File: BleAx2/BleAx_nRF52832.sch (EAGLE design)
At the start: 42 parts, among them CN1 6p-2.54, J1 2.0MM-90D, U1 NRF52832, U2 MCP73832T-2ACI/OT-SOT23-5, U4 MIC5225-3.3, X1 FA-128, X2 32.768kHz

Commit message: halfway?
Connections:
- net BTTN_01: now also U1.P0.10/NFC2@12; no longer U1.P0.31@43
- net LIS_CS: now also U1.P0.06@08; no longer U1.P0.07@09
- net LIS_INT1: now also U1.P0.05/AIN3@07; no longer U1.P0.06@08
- net MISO_01: now also U1.P0.07@09; no longer U1.P0.08@10
- net MOSI_01: now also U1.P0.08@10; no longer U1.P0.09/NFC1@11
- net SCK_01: now also U1.P0.09/NFC1@11; no longer U1.P0.10/NFC2@12
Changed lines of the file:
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@@
 </segment>
 <segment>
-<wire x1="88.9" y1="78.74" x2="66.04" y2="78.74" width="0.1524" layer="91"/>
-<pinref part="U1" gate="U$1" pin="P0.08@10"/>
-<label x="66.04" y="78.74" size="1.27" layer="95" rot="R180" xref="yes"/>
+<wire x1="88.9" y1="81.28" x2="63.5" y2="81.28" width="0.1524" layer="91"/>
+<pinref part="U1" gate="U$1" pin="P0.07@09"/>
+<label x="63.5" y="81.28" size="1.27" layer="95" rot="R180" xref="yes"/>
 </segment>
 </net>
@@
 </segment>
 <segment>
-<wire x1="66.04" y1="73.66" x2="88.9" y2="73.66" width="0.1524" layer="91"/>
-<pinref part="U1" gate="U$1" pin="P0.10/NFC2@12"/>
-<label x="66.04" y="73.66" size="1.27" layer="95" rot="R180" xref="yes"/>
+<wire x1="63.5" y1="76.2" x2="88.9" y2="76.2" width="0.1524" layer="91"/>
+<pinref part="U1" gate="U$1" pin="P0.09/NFC1@11"/>
+<label x="63.5" y="76.2" size="1.27" layer="95" rot="R180" xref="yes"/>
 </segment>
 </net>
@@
 </segment>
 <segment>
-<wire x1="66.04" y1="76.2" x2="88.9" y2="76.2" width="0.1524" layer="91"/>
-<pinref part="U1" gate="U$1" pin="P0.09/NFC1@11"/>
-<label x="66.04" y="76.2" size="1.27" layer="95" rot="R180" xref="yes"/>
+<wire x1="63.5" y1="78.74" x2="88.9" y2="78.74" width="0.1524" layer="91"/>
+<pinref part="U1" gate="U$1" pin="P0.08@10"/>
+<label x="63.5" y="78.74" size="1.27" layer="95" rot="R180" xref="yes"/>
 </segment>
 </net>
@@
 </segment>
 <segment>
-<wire x1="88.9" y1="81.28" x2="66.04" y2="81.28" width="0.1524" layer="91"/>
-<pinref part="U1" gate="U$1" pin="P0.07@09"/>
-<label x="66.04" y="81.28" size="1.27" layer="95" rot="R180" xref="yes"/>
+<wire x1="88.9" y1="83.82" x2="63.5" y2="83.82" width="0.1524" layer="91"/>
+<pinref part="U1" gate="U$1" pin="P0.06@08"/>
+<label x="63.5" y="83.82" size="1.27" layer="95" rot="R180" xref="yes"/>
 </segment>
 </net>
@@
 </segment>
 <segment>
-<wire x1="66.04" y1="83.82" x2="88.9" y2="83.82" width="0.1524" layer="91"/>
-<pinref part="U1" gate="U$1" pin="P0.06@08"/>
-<label x="66.04" y="83.82" size="1.27" layer="95" rot="R180" xref="yes"/>
+<wire x1="63.5" y1="86.36" x2="88.9" y2="86.36" width="0.1524" layer="91"/>
+<pinref part="U1" gate="U$1" pin="P0.05/AIN3@07"/>
+<label x="63.5" y="86.36" size="1.27" layer="95" rot="R180" xref="yes"/>
 </segment>
 </net>
@@
 <net name="BTTN_01" class="0">
 <segment>
-<pinref part="U1" gate="U$1" pin="P0.31@43"/>
-<wire x1="119.38" y1="119.38" x2="119.38" y2="124.46" width="0.1524" layer="91"/>
-<label x="119.38" y="124.46" size="1.27" layer="95" rot="R90" xref="yes"/>
-</segment>
-<segment>
 <pinref part="R8" gate="R$1" pin="1"/>
 <wire x1="200.66" y1="149.86" x2="205.74" y2="149.86" width="0.1524" layer="91"/>
 <label x="200.66" y="149.86" size="1.27" layer="95" rot="R180" xref="yes"/>
 </segment>
+<segment>
+<wire x1="81.28" y1="73.66" x2="88.9" y2="73.66" width="0.1524" layer="91"/>
+<pinref part="U1" gate="U$1" pin="P0.10/NFC2@12"/>
+<label x="81.28" y="73.66" size="1.27" layer="95" rot="R180" xref="yes"/>
+</segment>
 </net>

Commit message: half half evolve
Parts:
- D1: value LED -> LED_BLUE
- D3: value LED -> LED_CHARGE
- D4: value LED -> LED_GREEN
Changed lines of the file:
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@@
 <part name="C12" library="Nordic_misc" deviceset="CAPACITOR" device="_0402_N" value="12pF"/>
 <part name="GND22" library="supply1" deviceset="GND" device=""/>
-<part name="D3" library="Nordic_misc" deviceset="LED" device=""/>
+<part name="D3" library="Nordic_misc" deviceset="LED" device="" value="LED_CHARGE"/>
 <part name="R11" library="Nordic_misc" deviceset="RESISTOR" device="_0402_N" value="1k"/>
 <part name="U$3" library="microbuilder" deviceset="ACCEL_LIS3DHTR" device=""/>
@@
 <part name="GND21" library="supply1" deviceset="GND" device=""/>
 <part name="VDD_NRF10" library="supply2" deviceset="VCC" device="" value="VDD_P3V3"/>
-<part name="D1" library="Nordic_misc" deviceset="LED" device=""/>
+<part name="D1" library="Nordic_misc" deviceset="LED" device="" value="LED_BLUE"/>
 <part name="R2" library="Nordic_misc" deviceset="RESISTOR" device="_0402_N" value="1k"/>
-<part name="D4" library="Nordic_misc" deviceset="LED" device=""/>
+<part name="D4" library="Nordic_misc" deviceset="LED" device="" value="LED_GREEN"/>
 <part name="R3" library="Nordic_misc" deviceset="RESISTOR" device="_0402_N" value="1k"/>
 <part name="GND11" library="supply1" deviceset="GND" device=""/>

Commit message: usb_change
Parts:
- removed U$1: MICRO-USB-RECEPTACLE47589-0001, con-molex-usb:MICRO-USB-RECEPTACLE47589-0001
- added U$4: MICRO-USB-RECEPTACLE_MY, con-molex-usb_my:MICRO-USB-RECEPTACLE_MY
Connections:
- net GND: now also U$4.5; no longer U$1.5
- net VCC_P5V0_USB: now also U$4.1; no longer U$1.1
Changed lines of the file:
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@@
 <part name="R3" library="Nordic_misc" deviceset="RESISTOR" device="_0402_N" value="1k"/>
 <part name="GND11" library="supply1" deviceset="GND" device=""/>
-<part name="U$1" library="con-molex-usb" deviceset="MICRO-USB-RECEPTACLE" device="47589-0001"/>
 <part name="X1" library="crystals" deviceset="FA-128" device=""/>
 <part name="R4" library="Nordic_misc" deviceset="RESISTOR" device="_0402_N" value="100k"/>
@@
 <part name="GND25" library="supply1" deviceset="GND" device=""/>
 <part name="GND26" library="supply1" deviceset="GND" device=""/>
+<part name="U$4" library="con-molex-usb_my" deviceset="MICRO-USB-RECEPTACLE_MY" device=""/>
 </parts>
 <sheets>
@@
 <instance part="J1" gate="G$1" x="111.76" y="46.99"/>
 <instance part="VDD_BATT1" gate="G$1" x="99.06" y="53.34"/>
-<instance part="U$1" gate="G$1" x="33.02" y="43.18" rot="MR0"/>
+<instance part="U$4" gate="G$1" x="30.48" y="40.64" rot="MR0"/>
 </instances>
 <busses>
@@
 <wire x1="48.26" y1="38.1" x2="40.64" y2="38.1" width="0.1524" layer="91"/>
 <junction x="40.64" y="38.1"/>
-<pinref part="U$1" gate="G$1" pin="5"/>
-<wire x1="40.64" y1="38.1" x2="38.1" y2="38.1" width="0.1524" layer="91"/>
+<wire x1="40.64" y1="38.1" x2="35.56" y2="38.1" width="0.1524" layer="91"/>
+<pinref part="U$4" gate="G$1" pin="5"/>
 </segment>
 <segment>
@@
 <pinref part="D3" gate="D$1" pin="A"/>
 <pinref part="U2" gate="G$1" pin="VDD"/>
-<wire x1="38.1" y1="48.26" x2="45.72" y2="48.26" width="0.1524" layer="91"/>
-<pinref part="U$1" gate="G$1" pin="1"/>
 <wire x1="45.72" y1="48.26" x2="60.96" y2="48.26" width="0.1524" layer="91"/>
 <wire x1="71.12" y1="27.94" x2="45.72" y2="27.94" width="0.1524" layer="91"/>
 <wire x1="45.72" y1="27.94" x2="45.72" y2="48.26" width="0.1524" layer="91"/>
 <junction x="45.72" y="48.26"/>
-</segment>
-</net>
+<wire x1="45.72" y1="48.26" x2="35.56" y2="48.26" width="0.1524" layer="91"/>
+<pinref part="U$4" gate="G$1" pin="1"/>
+</segment>
+</net>

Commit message: pravki and gerbers
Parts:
- added TP1, TP2: TPSQTP08R, testpad:TPSQTP08R
- U$2: value SST26VF -> SST26VF064B-104I/SM
- U$3: value (none) -> LIS3DH
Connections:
- net DEC1 renamed N$13
- new net N$11: TP1.TP, U1.P0.19@22
- new net N$12: TP2.TP, U1.P0.20@23
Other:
- note removed: "Power sources"
- note removed: "Power supply"
- moved on the sheet: BTN2, C1, C11, C12, C2, C4, C7, C9, CN1, D1, D4, L2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

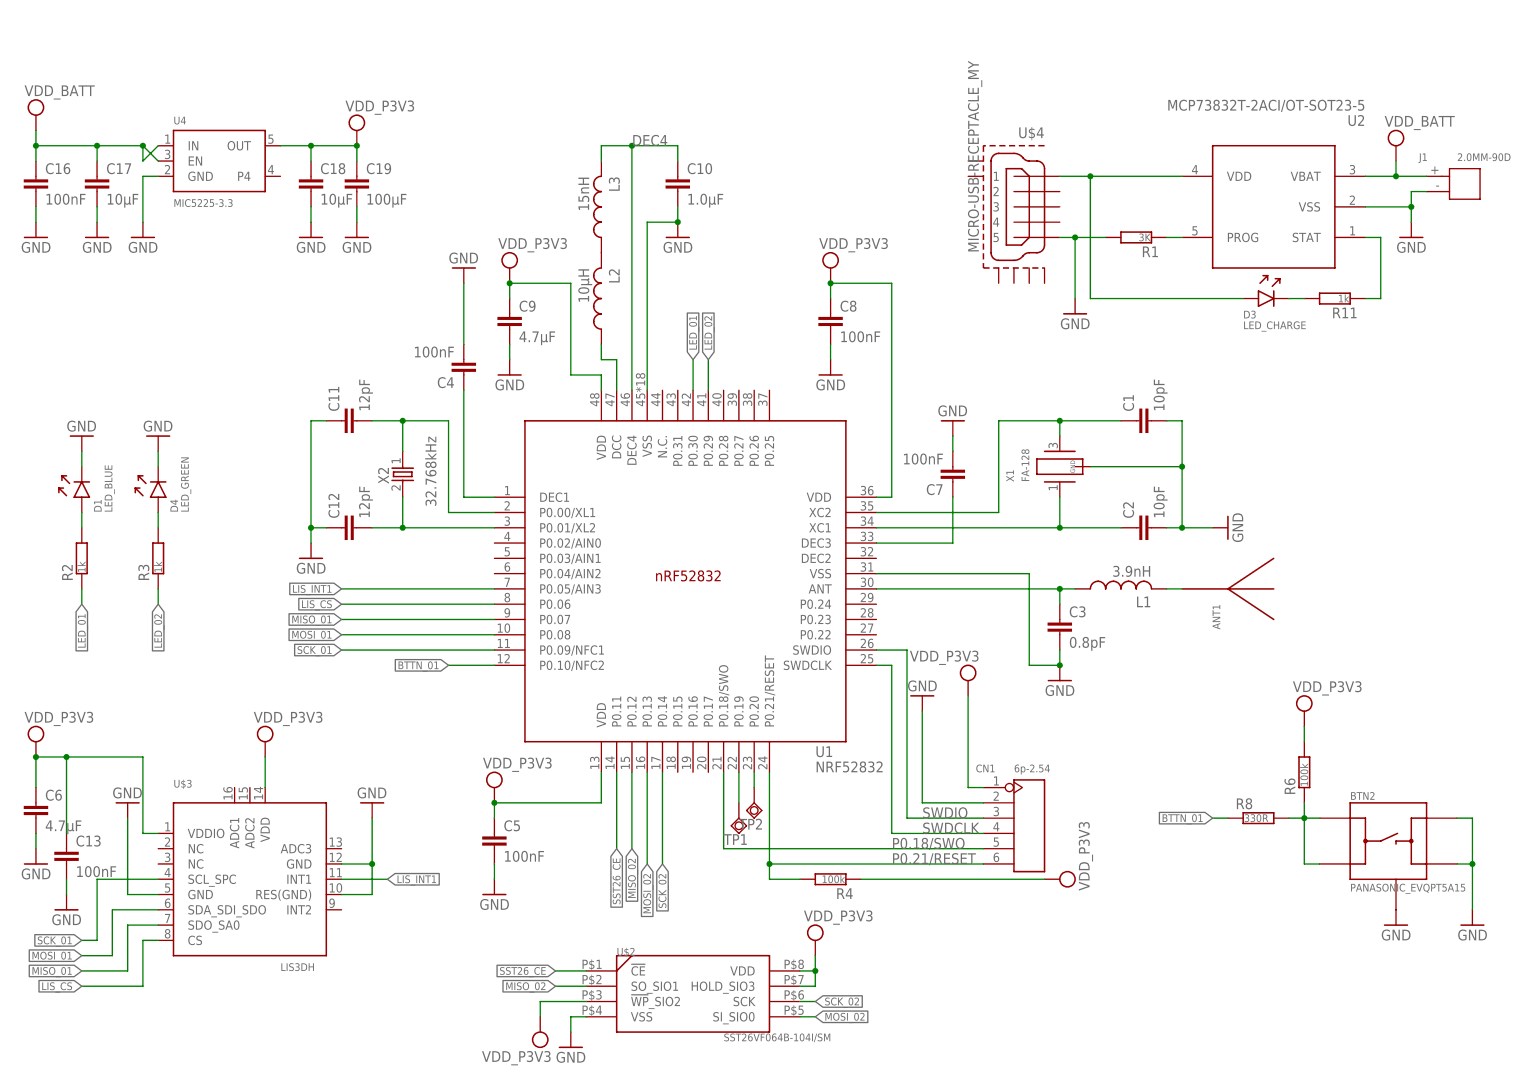
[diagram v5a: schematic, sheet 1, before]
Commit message: resistor value changed
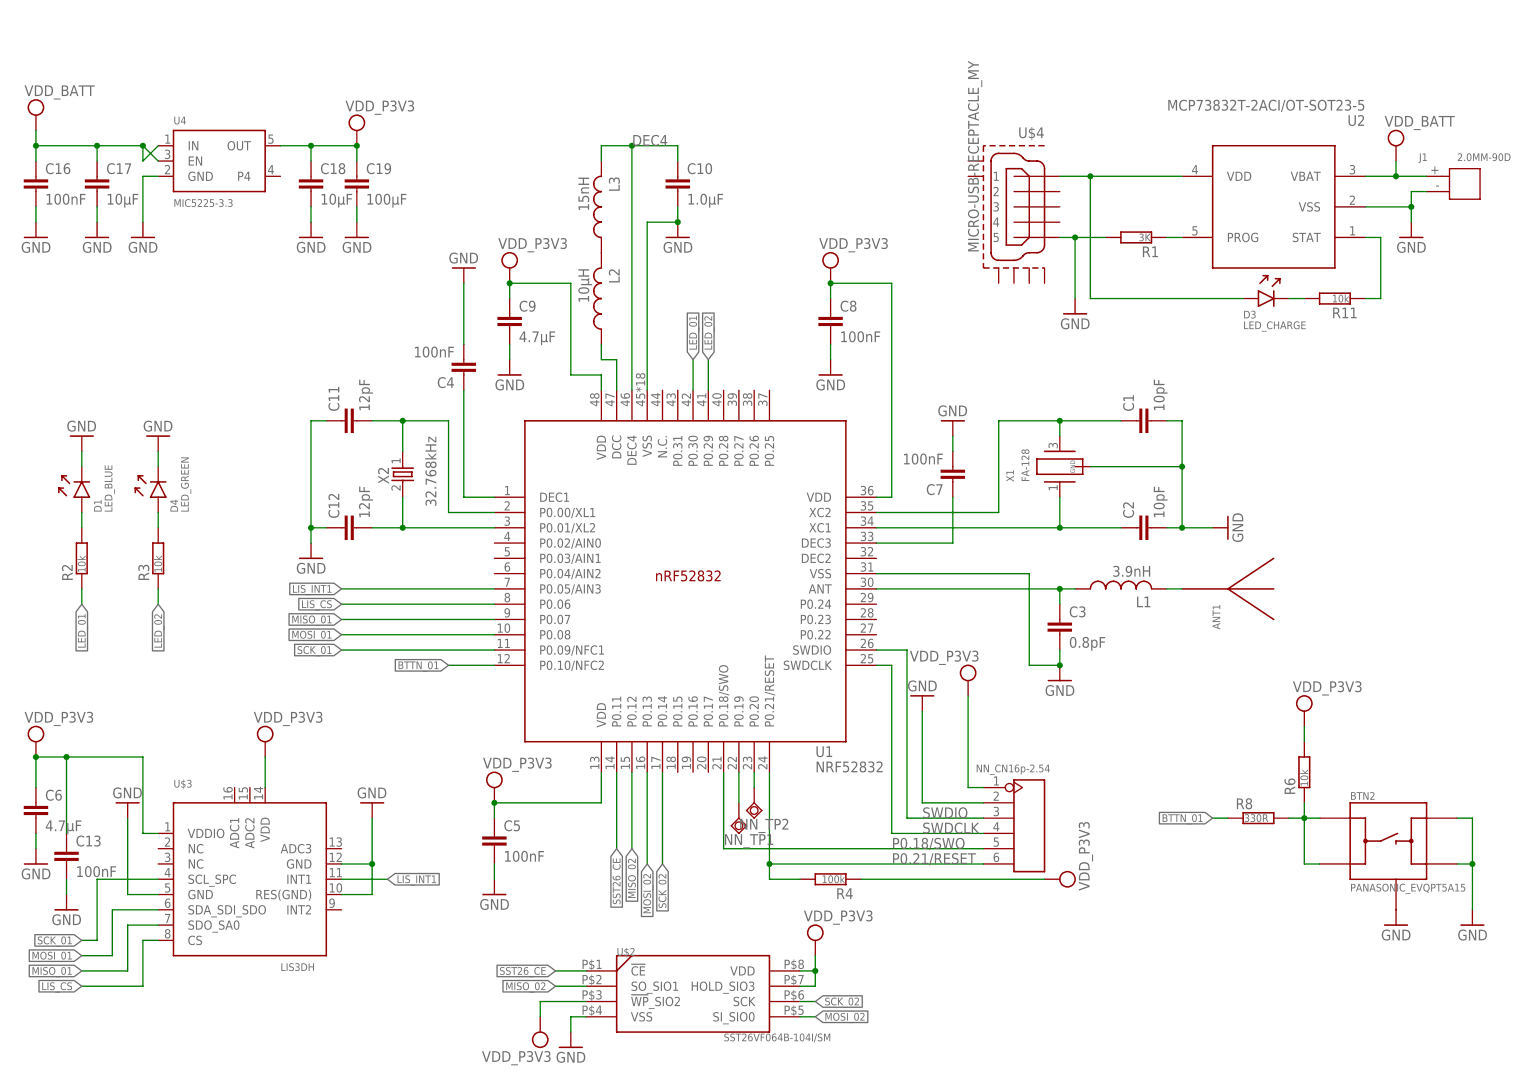
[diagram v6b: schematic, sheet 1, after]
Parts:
- R11, R2, R3: value 1k -> 10k
- R6: value 100k -> 10k
- renumbered CN1 to NN_CN1, TP1 to NN_TP1, TP2 to NN_TP2
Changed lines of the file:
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@@
 <part name="GND22" library="supply1" deviceset="GND" device=""/>
 <part name="D3" library="Nordic_misc" deviceset="LED" device="" value="LED_CHARGE"/>
-<part name="R11" library="Nordic_misc" deviceset="RESISTOR" device="_0402_N" value="1k"/>
+<part name="R11" library="Nordic_misc" deviceset="RESISTOR" device="_0402_N" value="10k"/>
 <part name="U$3" library="microbuilder" deviceset="ACCEL_LIS3DHTR" device="" value="LIS3DH"/>
 <part name="GND8" library="supply1" deviceset="GND" device=""/>
@@
 <part name="VDD_NRF8" library="supply2" deviceset="VCC" device="" value="VDD_P3V3"/>
 <part name="GND12" library="supply1" deviceset="GND" device=""/>
-<part name="CN1" library="Seeed-OPL-Connector" deviceset="DIP-BLACK-FEMALE-HEADER-VERT(6P-2.54)" device="" value="6p-2.54"/>
+<part name="NN_CN1" library="Seeed-OPL-Connector" deviceset="DIP-BLACK-FEMALE-HEADER-VERT(6P-2.54)" device="" value="6p-2.54"/>
 <part name="GND13" library="supply1" deviceset="GND" device=""/>
 <part name="C13" library="Nordic_misc" deviceset="CAPACITOR" device="_0402_N" value="100nF"/>
@@
 <part name="VDD_NRF10" library="supply2" deviceset="VCC" device="" value="VDD_P3V3"/>
 <part name="D1" library="Nordic_misc" deviceset="LED" device="" value="LED_BLUE"/>
-<part name="R2" library="Nordic_misc" deviceset="RESISTOR" device="_0402_N" value="1k"/>
+<part name="R2" library="Nordic_misc" deviceset="RESISTOR" device="_0402_N" value="10k"/>
 <part name="D4" library="Nordic_misc" deviceset="LED" device="" value="LED_GREEN"/>
-<part name="R3" library="Nordic_misc" deviceset="RESISTOR" device="_0402_N" value="1k"/>
+<part name="R3" library="Nordic_misc" deviceset="RESISTOR" device="_0402_N" value="10k"/>
 <part name="GND11" library="supply1" deviceset="GND" device=""/>
 <part name="X1" library="crystals" deviceset="FA-128" device=""/>
@@
 <part name="VDD_NRF11" library="supply2" deviceset="VCC" device="" value="VDD_P3V3"/>
 <part name="BTN2" library="Nordic_misc" deviceset="PANASONIC_EVQPT5A15" device=""/>
-<part name="R6" library="Nordic_misc" deviceset="RESISTOR" device="_0402_N" value="100k"/>
+<part name="R6" library="Nordic_misc" deviceset="RESISTOR" device="_0402_N" value="10k"/>
 <part name="VDD_NRF14" library="supply2" deviceset="VCC" device="" value="VDD_P3V3"/>
 <part name="GND23" library="supply1" deviceset="GND" device=""/>
@@
 <part name="GND26" library="supply1" deviceset="GND" device=""/>
 <part name="U$4" library="con-molex-usb_my" deviceset="MICRO-USB-RECEPTACLE_MY" device=""/>
-<part name="TP1" library="testpad" deviceset="TPSQ" device="TP08R"/>
-<part name="TP2" library="testpad" deviceset="TPSQ" device="TP08R"/>
+<part name="NN_TP1" library="testpad" deviceset="TPSQ" device="TP08R"/>
+<part name="NN_TP2" library="testpad" deviceset="TPSQ" device="TP08R"/>
 </parts>
 <sheets>
@@
 <instance part="VDD_NRF8" gate="G$1" x="50.8" y="60.96"/>
 <instance part="GND12" gate="1" x="27.94" y="50.8" rot="MR180"/>
-<instance part="CN1" gate="G$1" x="177.8" y="46.99"/>
+<instance part="NN_CN1" gate="G$1" x="177.8" y="46.99"/>
 <instance part="GND13" gate="1" x="17.78" y="33.02" rot="MR0"/>
 <instance part="C13" gate="C$1" x="17.78" y="43.18"/>
@@
 <instance part="GND25" gate="1" x="20.32" y="111.76" rot="MR180"/>
 <instance part="GND26" gate="1" x="33.02" y="111.76" rot="MR180"/>
-<instance part="TP1" gate="G$1" x="129.54" y="48.26"/>
-<instance part="TP2" gate="G$1" x="132.08" y="50.8"/>
+<instance part="NN_TP1" gate="G$1" x="129.54" y="48.26"/>
+<instance part="NN_TP2" gate="G$1" x="132.08" y="50.8"/>
 <instance part="GND22" gate="1" x="185.42" y="132.08" rot="MR0"/>
 <instance part="D3" gate="D$1" x="218.44" y="134.62"/>
@@
 <wire x1="160.02" y1="66.04" x2="160.02" y2="50.8" width="0.1524" layer="91"/>
 <wire x1="160.02" y1="50.8" x2="170.18" y2="50.8" width="0.1524" layer="91"/>
-<pinref part="CN1" gate="G$1" pin="2"/>
+<pinref part="NN_CN1" gate="G$1" pin="2"/>
 </segment>
 <segment>
@@
 <wire x1="167.64" y1="68.58" x2="167.64" y2="53.34" width="0.1524" layer="91"/>
 <wire x1="167.64" y1="53.34" x2="170.18" y2="53.34" width="0.1524" layer="91"/>
-<pinref part="CN1" gate="G$1" pin="1"/>
+<pinref part="NN_CN1" gate="G$1" pin="1"/>
 </segment>
 <segment>
@@
 <label x="154.94" y="43.18" size="1.778" layer="95"/>
 <wire x1="170.18" y1="43.18" x2="127" y2="43.18" width="0.1524" layer="91"/>
-<pinref part="CN1" gate="G$1" pin="5"/>
+<pinref part="NN_CN1" gate="G$1" pin="5"/>
 </segment>
 </net>
@@
 <label x="154.94" y="40.64" size="1.778" layer="95"/>
 <wire x1="170.18" y1="40.64" x2="134.62" y2="40.64" width="0.1524" layer="91"/>
-<pinref part="CN1" gate="G$1" pin="6"/>
+<pinref part="NN_CN1" gate="G$1" pin="6"/>
 <wire x1="134.62" y1="40.64" x2="134.62" y2="38.1" width="0.1524" layer="91"/>
 <pinref part="R4" gate="R$1" pin="2"/>
@@
 <wire x1="154.94" y1="45.72" x2="170.18" y2="45.72" width="0.1524" layer="91"/>
 <label x="160.02" y="45.72" size="1.778" layer="95"/>
-<pinref part="CN1" gate="G$1" pin="4"/>
+<pinref part="NN_CN1" gate="G$1" pin="4"/>
 </segment>
 </net>
@@
 <wire x1="157.48" y1="48.26" x2="170.18" y2="48.26" width="0.1524" layer="91"/>
 <label x="160.02" y="48.26" size="1.778" layer="95"/>
-<pinref part="CN1" gate="G$1" pin="3"/>
+<pinref part="NN_CN1" gate="G$1" pin="3"/>
 </segment>
 </net>
@@
 <segment>
 <pinref part="U1" gate="U$1" pin="P0.19@22"/>
-<pinref part="TP1" gate="G$1" pin="TP"/>
+<pinref part="NN_TP1" gate="G$1" pin="TP"/>
 <wire x1="129.54" y1="50.8" x2="129.54" y2="55.88" width="0.1524" layer="91"/>
 </segment>
@@
 <pinref part="U1" gate="U$1" pin="P0.20@23"/>
 <wire x1="132.08" y1="53.34" x2="132.08" y2="55.88" width="0.1524" layer="91"/>
-<pinref part="TP2" gate="G$1" pin="TP"/>
-</segment>
-</net>
+<pinref part="NN_TP2" gate="G$1" pin="TP"/>
+</segment>
+</net>
